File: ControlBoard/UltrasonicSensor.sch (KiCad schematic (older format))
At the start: 34 parts, among them J6 Ultrasonic Transmitter, J7 Ultrasonic Receiver, Q2 2N3904, U3 LM358, U4 LM358

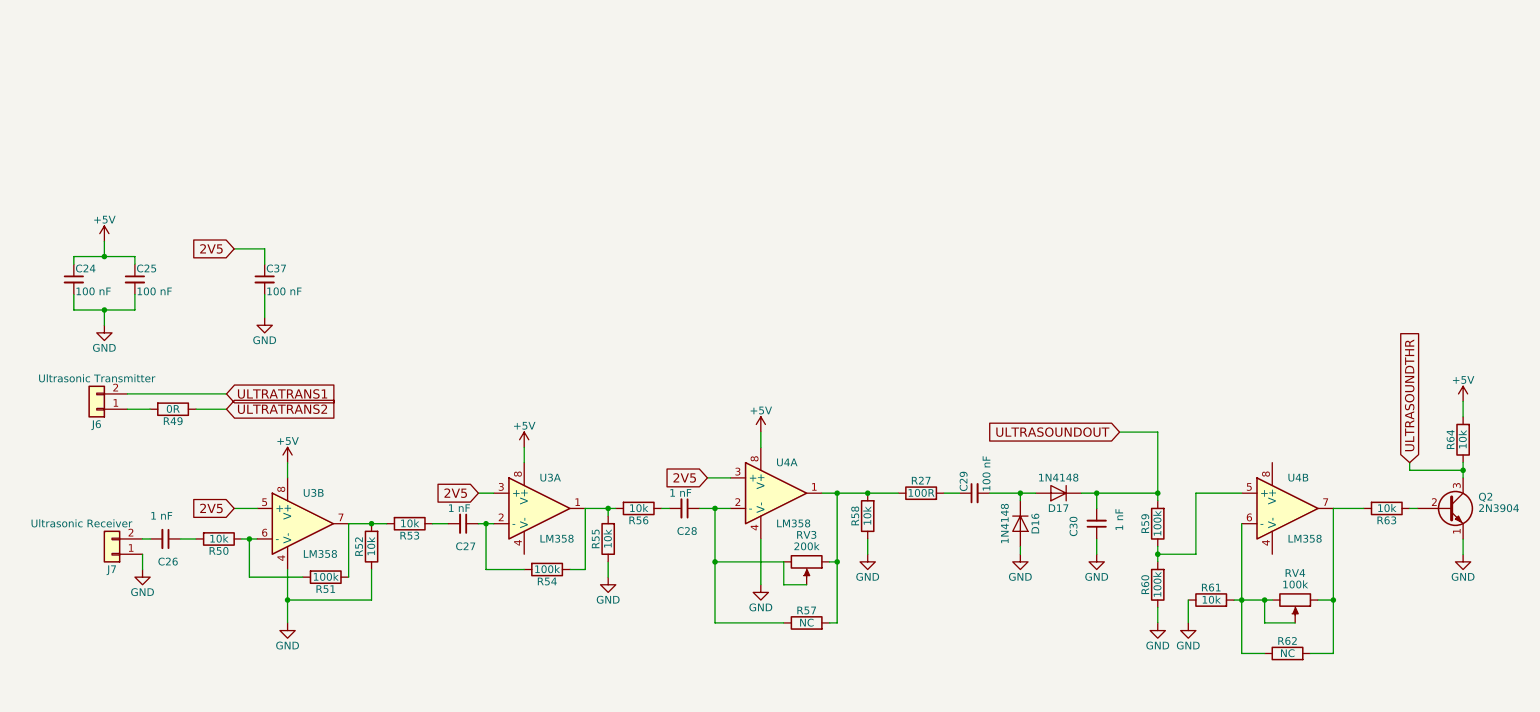
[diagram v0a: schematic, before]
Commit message: Added CAD models
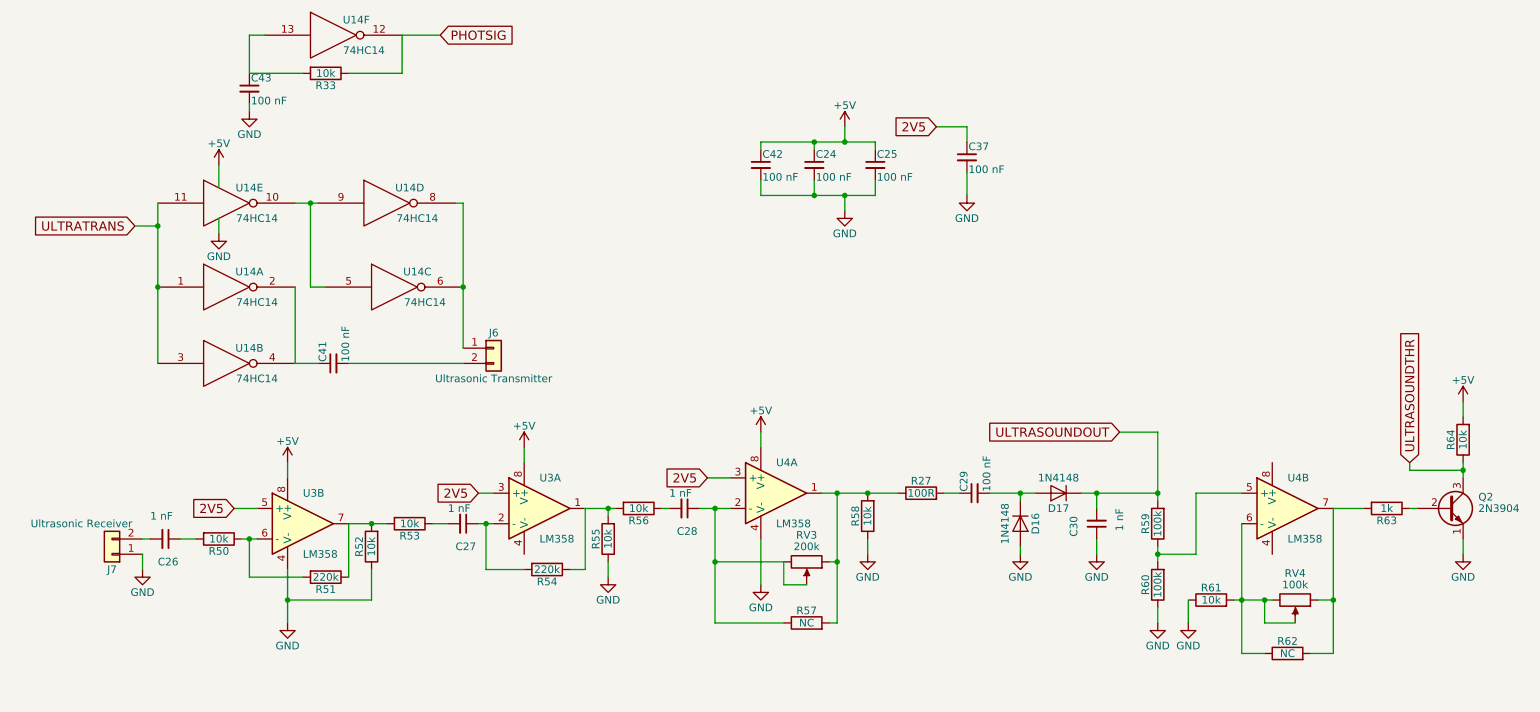
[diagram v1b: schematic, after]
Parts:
- removed R49: 0R, Resistors_THT:R_Axial_DIN0207_L6.3mm_D2.5mm_P7.62mm_Horizontal, symbol R
- added C41, C42, C43: 100 nF, Capacitors_THT:C_Disc_D5.0mm_W2.5mm_P2.50mm, symbol C_Small
- added R33: 10k, Resistors_THT:R_Axial_DIN0207_L6.3mm_D2.5mm_P7.62mm_Horizontal, symbol R
- added U14: 74HC14, Housings_DIP:DIP-14_W7.62mm_Socket, symbol 74HC14
- R51, R54: value 100k -> 220k
- R63: value 10k -> 1k
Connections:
- net +5V: now also C42.1, U14.14 (VCC), U14.14 (VCC), U14.14 (VCC), U14.14 (VCC), U14.14 (VCC), U14.14 (VCC)
- net GND: now also C42.2, C43.2, U14.7 (GND), U14.7 (GND), U14.7 (GND), U14.7 (GND), U14.7 (GND), U14.7 (GND)
- net at J6.1 (Pin_1): now also U14.6, U14.8
- net ULTRATRANS1: no longer names the net of J6.2 (Pin_2)
- net ULTRATRANS1: now also C41.2
- new net: C41.1, U14.2, U14.4
- new net: C43.1, R33.2, U14.13
- new net: U14.10, U14.5, U14.9
- new net PHOTSIG: R33.1, U14.12
- new net ULTRATRANS: U14.1, U14.11, U14.3
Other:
- moved on the sheet: C24, C25, C37, J6

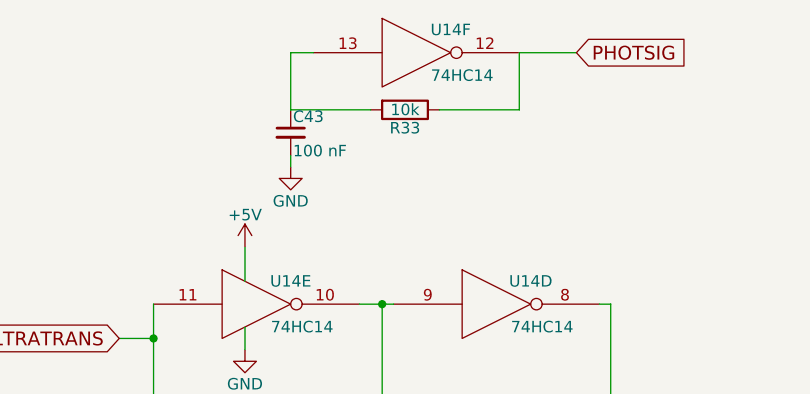
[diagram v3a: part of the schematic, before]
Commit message: Begin code for controlling robot with command line
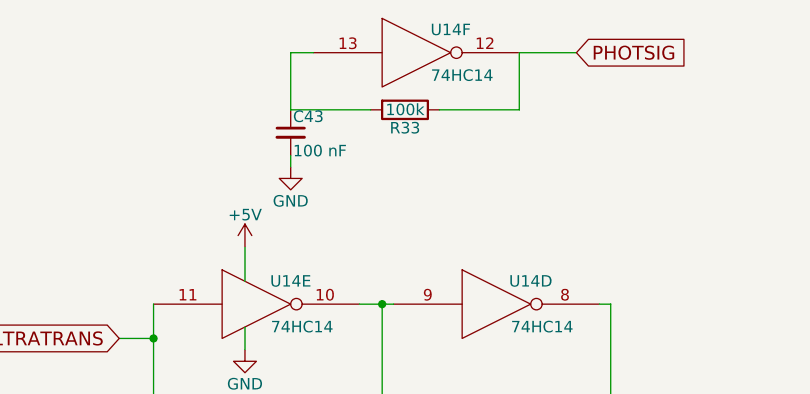
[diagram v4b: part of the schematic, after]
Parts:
- R33: value 10k -> 100k
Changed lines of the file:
@@
 P 2600 1200
 F 0 "R33" V 2680 1200 50  0000 C CNN
-F 1 "10k" V 2600 1200 50  0000 C CNN
+F 1 "100k" V 2600 1200 50  0000 C CNN
 F 2 "Resistors_THT:R_Axial_DIN0207_L6.3mm_D2.5mm_P7.62mm_Horizontal" V 2530 1200 50  0001 C CNN
 F 3 "" H 2600 1200 50  0001 C CNN

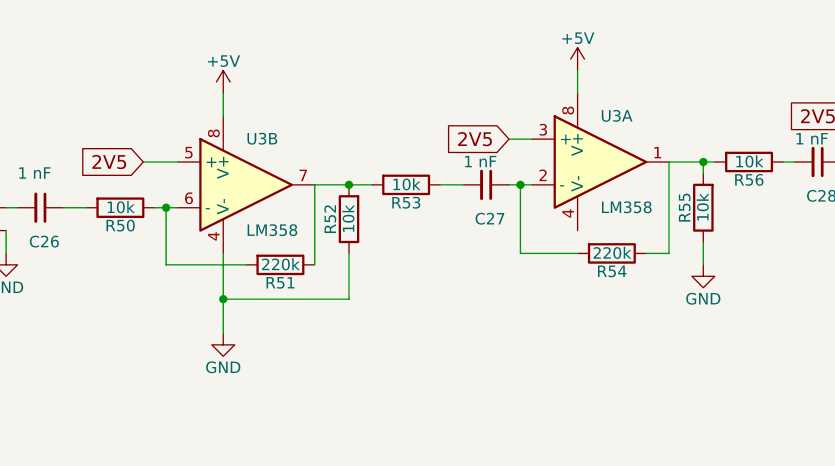
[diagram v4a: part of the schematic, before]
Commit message: Added some filter capacitors
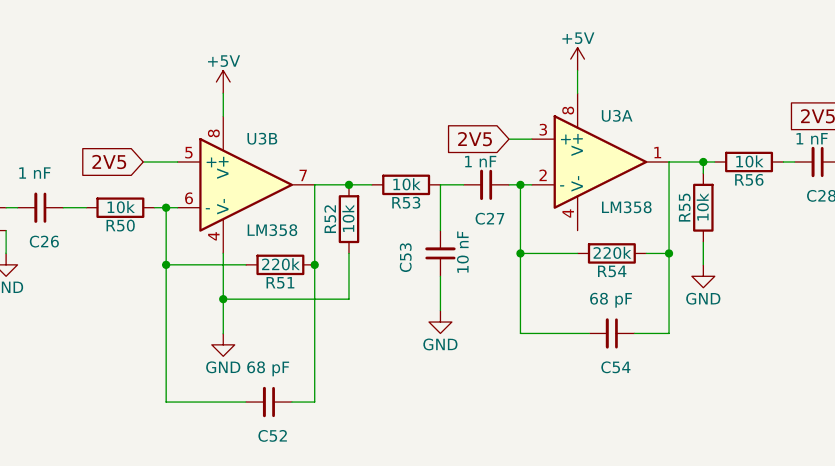
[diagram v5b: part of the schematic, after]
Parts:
- added C52, C54: 68 pF, Capacitors_THT:C_Disc_D5.0mm_W2.5mm_P5.00mm, symbol C_Small
- added C53: 10 nF, Capacitors_THT:C_Disc_D5.0mm_W2.5mm_P5.00mm, symbol C_Small
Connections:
- net GND: now also C53.1
- net at R50.1, R51.2, U3.6 (-): now also C52.2
- net at R51.1, R52.2, R53.2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: now also C52.1
- net at R54.1, R55.2, R56.2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: now also C54.1
- net at C27.1, R54.2, U3.2 (-): now also C54.2
- net at C27.2, R53.1: now also C53.2
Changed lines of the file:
@@
 $EndComp
 $Comp
-L +5V #PWR93
+L +5V #PWR95
 U 1 1 614A336E
 P 2350 3750
-F 0 "#PWR93" H 2350 3600 50  0001 C CNN
+F 0 "#PWR95" H 2350 3600 50  0001 C CNN
 F 1 "+5V" H 2350 3890 50  0000 C CNN
 F 2 "" H 2350 3750 50  0001 C CNN
@@
 $EndComp
 $Comp
-L GND #PWR94
+L GND #PWR96
 U 1 1 614A3393
 P 2350 4800
-F 0 "#PWR94" H 2350 4550 50  0001 C CNN
+F 0 "#PWR96" H 2350 4550 50  0001 C CNN
 F 1 "GND" H 2350 4650 50  0000 C CNN
 F 2 "" H 2350 4800 50  0001 C CNN
@@
 $EndComp
 $Comp
-L GND #PWR89
+L GND #PWR91
 U 1 1 614A352A
 P 1400 4450
-F 0 "#PWR89" H 1400 4200 50  0001 C CNN
+F 0 "#PWR91" H 1400 4200 50  0001 C CNN
 F 1 "GND" H 1400 4300 50  0000 C CNN
 F 2 "" H 1400 4450 50  0001 C CNN
@@
 $EndComp
 $Comp
-L +5V #PWR99
+L +5V #PWR102
 U 1 1 614A3B3B
 P 6000 1550
-F 0 "#PWR99" H 6000 1400 50  0001 C CNN
+F 0 "#PWR102" H 6000 1400 50  0001 C CNN
 F 1 "+5V" H 6000 1690 50  0000 C CNN
 F 2 "" H 6000 1550 50  0001 C CNN
@@
 $EndComp
 $Comp
-L GND #PWR100
+L GND #PWR103
 U 1 1 614A3B80
 P 6000 2100
-F 0 "#PWR100" H 6000 1850 50  0001 C CNN
+F 0 "#PWR103" H 6000 1850 50  0001 C CNN
 F 1 "GND" H 6000 1950 50  0000 C CNN
 F 2 "" H 6000 2100 50  0001 C CNN
@@
 2V5
 $Comp
-L +5V #PWR95
+L +5V #PWR98
 U 1 1 614A4DD3
 P 3900 3650
-F 0 "#PWR95" H 3900 3500 50  0001 C CNN
+F 0 "#PWR98" H 3900 3500 50  0001 C CNN
 F 1 "+5V" H 3900 3790 50  0000 C CNN
 F 2 "" H 3900 3650 50  0001 C CNN
@@
 $EndComp
 $Comp
-L +5V #PWR97
+L +5V #PWR100
 U 1 1 614A515C
 P 5450 3550
-F 0 "#PWR97" H 5450 3400 50  0001 C CNN
+F 0 "#PWR100" H 5450 3400 50  0001 C CNN
 F 1 "+5V" H 5450 3690 50  0000 C CNN
 F 2 "" H 5450 3550 50  0001 C CNN
@@
 $EndComp
 $Comp
-L GND #PWR98
+L GND #PWR101
 U 1 1 614B0FF4
 P 5450 4550
-F 0 "#PWR98" H 5450 4300 50  0001 C CNN
+F 0 "#PWR101" H 5450 4300 50  0001 C CNN
 F 1 "GND" H 5450 4400 50  0000 C CNN
 F 2 "" H 5450 4550 50  0001 C CNN
@@
 $EndComp
 $Comp
-L GND #PWR96
+L GND #PWR99
 U 1 1 614B13F0
 P 4450 4500
-F 0 "#PWR96" H 4450 4250 50  0001 C CNN
+F 0 "#PWR99" H 4450 4250 50  0001 C CNN
 F 1 "GND" H 4450 4350 50  0000 C CNN
 F 2 "" H 4450 4500 50  0001 C CNN
@@
 $EndComp
 $Comp
-L GND #PWR101
+L GND #PWR104
 U 1 1 614B1531
 P 6150 4350
-F 0 "#PWR101" H 6150 4100 50  0001 C CNN
+F 0 "#PWR104" H 6150 4100 50  0001 C CNN
 F 1 "GND" H 6150 4200 50  0000 C CNN
 F 2 "" H 6150 4350 50  0001 C CNN
@@
 $EndComp
 $Comp
-L GND #PWR103
+L GND #PWR106
 U 1 1 614B1897
 P 7150 4350
-F 0 "#PWR103" H 7150 4100 50  0001 C CNN
+F 0 "#PWR106" H 7150 4100 50  0001 C CNN
 F 1 "GND" H 7150 4200 50  0000 C CNN
 F 2 "" H 7150 4350 50  0001 C CNN
@@
 $EndComp
 $Comp
-L GND #PWR104
+L GND #PWR107
 U 1 1 614B1BD3
 P 7650 4350
-F 0 "#PWR104" H 7650 4100 50  0001 C CNN
+F 0 "#PWR107" H 7650 4100 50  0001 C CNN
 F 1 "GND" H 7650 4200 50  0000 C CNN
 F 2 "" H 7650 4350 50  0001 C CNN
@@
 $EndComp
 $Comp
-L GND #PWR105
+L GND #PWR108
 U 1 1 614B1EB6
 P 8050 4800
-F 0 "#PWR105" H 8050 4550 50  0001 C CNN
+F 0 "#PWR108" H 8050 4550 50  0001 C CNN
 F 1 "GND" H 8050 4650 50  0000 C CNN
 F 2 "" H 8050 4800 50  0001 C CNN
@@
 $EndComp
 $Comp
-L GND #PWR106
+L GND #PWR109
 U 1 1 614B61A2
 P 8250 4800
-F 0 "#PWR106" H 8250 4550 50  0001 C CNN
+F 0 "#PWR109" H 8250 4550 50  0001 C CNN
 F 1 "GND" H 8250 4650 50  0000 C CNN
 F 2 "" H 8250 4800 50  0001 C CNN
@@
 $EndComp
 $Comp
-L GND #PWR108
+L GND #PWR111
 U 1 1 614B698E
 P 10050 4350
-F 0 "#PWR108" H 10050 4100 50  0001 C CNN
+F 0 "#PWR111" H 10050 4100 50  0001 C CNN
 F 1 "GND" H 10050 4200 50  0000 C CNN
 F 2 "" H 10050 4350 50  0001 C CNN
@@
 $EndComp
 $Comp
-L +5V #PWR107
+L +5V #PWR110
 U 1 1 614B6BC6
 P 10050 3350
-F 0 "#PWR107" H 10050 3200 50  0001 C CNN
+F 0 "#PWR110" H 10050 3200 50  0001 C CNN
 F 1 "+5V" H 10050 3490 50  0000 C CNN
 F 2 "" H 10050 3350 50  0001 C CNN
@@
 $EndComp
 $Comp
-L GND #PWR102
+L GND #PWR105
 U 1 1 61490DC0
 P 6800 2000
-F 0 "#PWR102" H 6800 1750 50  0001 C CNN
+F 0 "#PWR105" H 6800 1750 50  0001 C CNN
 F 1 "GND" H 6800 1850 50  0000 C CNN
 F 2 "" H 6800 2000 50  0001 C CNN
@@
 	1650 4250 1750 4250
 Wire Wire Line
-	2750 4150 2750 4500
+	2750 4150 2750 5100
 Wire Wire Line
 	2450 4500 2100 4500
 Wire Wire Line
-	2100 4500 2100 4250
+	2100 4250 2100 5100
 Connection ~ 2100 4250
 Wire Wire Line
@@
 	3900 3650 3900 3750
 Wire Wire Line
-	4300 4050 4300 4450
+	4300 4050 4300 4800
 Wire Wire Line
 	4300 4450 4200 4450
 Wire Wire Line
-	3650 4150 3650 4450
+	3650 4150 3650 4800
 Wire Wire Line
 	3650 4450 3900 4450
@@
 	6750 3950 6650 3950
 $Comp
-L +5V #PWR90
+L +5V #PWR92
 U 1 1 614B24F3
 P 1900 1800
-F 0 "#PWR90" H 1900 1650 50  0001 C CNN
+F 0 "#PWR92" H 1900 1650 50  0001 C CNN
 F 1 "+5V" H 1900 1940 50  0000 C CNN
 F 2 "" H 1900 1800 50  0001 C CNN
@@
 Connection ~ 5800 2000
 $Comp
-L GND #PWR91
+L GND #PWR93
 U 1 1 614B2A2C
 P 1900 2250
-F 0 "#PWR91" H 1900 2000 50  0001 C CNN
+F 0 "#PWR93" H 1900 2000 50  0001 C CNN
 F 1 "GND" H 1900 2100 50  0000 C CNN
 F 2 "" H 1900 2250 50  0001 C CNN
@@
 	3500 3100 2750 3100
 $Comp
-L GND #PWR92
+L GND #PWR94
 U 1 1 614D3C7D
 P 2100 1450
-F 0 "#PWR92" H 2100 1200 50  0001 C CNN
+F 0 "#PWR94" H 2100 1200 50  0001 C CNN
 F 1 "GND" H 2100 1300 50  0000 C CNN
 F 2 "" H 2100 1450 50  0001 C CNN
@@
 	1    0    0    -1
 $EndComp
+$Comp
+L C_Small C52
+U 1 1 61DD2E94
+P 2550 5100
+F 0 "C52" V 2700 5050 50  0000 L CNN
+F 1 "68 pF" V 2400 5000 50  0000 L CNN
+F 2 "Capacitors_THT:C_Disc_D5.0mm_W2.5mm_P5.00mm" H 2550 5100 50  0001 C CNN
+F 3 "" H 2550 5100 50  0001 C CNN
+	1    2550 5100
+	0    1    1    0
+$EndComp
+Wire Wire Line
+	2750 5100 2650 5100
+Connection ~ 2750 4500
+Wire Wire Line
+	2100 5100 2450 5100
+Connection ~ 2100 4500
+$Comp
+L C_Small C54
+U 1 1 61DD3271
+P 4050 4800
+F 0 "C54" V 4200 4750 50  0000 L CNN
+F 1 "68 pF" V 3900 4700 50  0000 L CNN
+F 2 "Capacitors_THT:C_Disc_D5.0mm_W2.5mm_P5.00mm" H 4050 4800 50  0001 C CNN
+F 3 "" H 4050 4800 50  0001 C CNN
+	1    4050 4800
+	0    1    1    0
+$EndComp
+Wire Wire Line
+	4300 4800 4150 4800
+Connection ~ 4300 4450
+Wire Wire Line
+	3650 4800 3950 4800
+Connection ~ 3650 4450
+$Comp
+L C_Small C53
+U 1 1 61DD55C3
+P 3300 4450
+F 0 "C53" V 3450 4400 50  0000 L CNN
+F 1 "10 nF" V 3200 4350 50  0000 L CNN
+F 2 "Capacitors_THT:C_Disc_D5.0mm_W2.5mm_P5.00mm" H 3300 4450 50  0001 C CNN
+F 3 "" H 3300 4450 50  0001 C CNN
+	1    3300 4450
+	-1   0    0    1
+$EndComp
+Wire Wire Line
+	3300 4350 3300 4150
+$Comp
+L GND #PWR97
+U 1 1 61DD5856
+P 3300 4700
+F 0 "#PWR97" H 3300 4450 50  0001 C CNN
+F 1 "GND" H 3300 4550 50  0000 C CNN
+F 2 "" H 3300 4700 50  0001 C CNN
+F 3 "" H 3300 4700 50  0001 C CNN
+	1    3300 4700
+	1    0    0    -1
+$EndComp
+Wire Wire Line
+	3300 4700 3300 4550
 $EndSCHEMATC
